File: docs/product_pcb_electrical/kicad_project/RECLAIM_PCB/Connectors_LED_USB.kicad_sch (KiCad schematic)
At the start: 15 parts, among them U11 PT4115

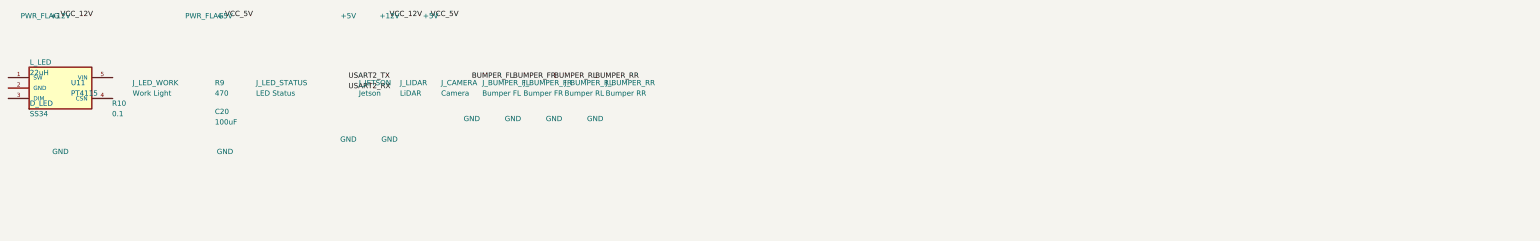
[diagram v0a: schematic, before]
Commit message: Add prototype schematic + tighten product layout to A3
Product: All 4 sub-sheets resized A2/A1→A3, components repositioned
into tight logical groups, duplicate K1/Q1 removed.

Prototype: New KiCad project with 3 hierarchical sheets
(Power, Teensy/Motor Control, Peripherals/Sensors), BOM, and
netlist reflecting as-built wiring: MD13C R3 + BTS7960 asymmetric
drivers, DC disconnect, 6-way fuse block, XINGYHENG servo buck.

Co-Authored-By: Claude Opus 4.6 <noreply@anthropic.com>
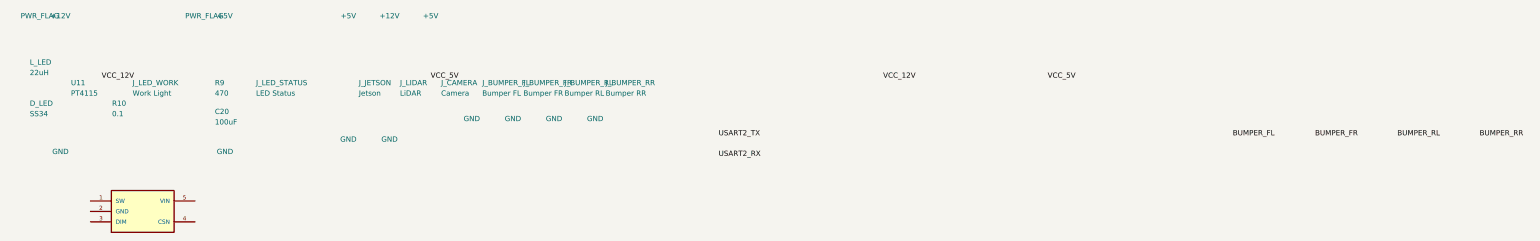
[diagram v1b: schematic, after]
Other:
- moved on the sheet: U11
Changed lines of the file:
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@@
 	(generator "eeschema")
 	(generator_version "10.0")
-	(paper "A2")
+	(paper "A3")
 	(title_block
 		(title "RECLAIM Product PCB - Connectors, LED, USB & Peripherals")
@@
 	(symbol
 		(lib_id "PT4115:PT4115")
-		(at 40 40 0)
+		(at 60 70 0)
 		(unit 1)
 		(body_style 1)
@@
 	(symbol
 		(lib_id "Device:L")
-		(at 30 35 0)
+		(at 45 52 0)
 		(unit 1)
 		(body_style 1)
@@
 	(symbol
 		(lib_id "Diode:SS34")
-		(at 30 45 0)
+		(at 45 95 0)
 		(unit 1)
 		(body_style 1)
@@
 	(symbol
 		(lib_id "Device:R")
-		(at 50 45 0)
+		(at 78 95 0)
 		(unit 1)
 		(body_style 1)
@@
 	(symbol
 		(lib_id "Connector_Generic:Conn_01x02")
-		(at 55 40 0)
+		(at 92 70 0)
 		(unit 1)
 		(body_style 1)
@@
 	(symbol
 		(lib_id "Device:R")
-		(at 75 40 0)
+		(at 130 55 0)
 		(unit 1)
 		(body_style 1)
@@
 	(symbol
 		(lib_id "Device:C")
-		(at 75 47 0)
+		(at 130 85 0)
 		(unit 1)
 		(body_style 1)
@@
 	(symbol
 		(lib_id "Connector_Generic:Conn_01x03")
-		(at 85 40 0)
+		(at 150 65 0)
 		(unit 1)
 		(body_style 1)
@@
 	(symbol
 		(lib_id "Connector_Generic:Conn_01x04")
-		(at 110 40 0)
+		(at 200 60 0)
 		(unit 1)
 		(body_style 1)
@@
 	(symbol
 		(lib_id "Connector_Generic:Conn_01x04")
-		(at 120 40 0)
+		(at 245 60 0)
 		(unit 1)
 		(body_style 1)
@@
 	(symbol
 		(lib_id "Connector_Generic:Conn_01x02")
-		(at 130 40 0)
+		(at 285 60 0)
 		(unit 1)
 		(body_style 1)
@@
 	(symbol
 		(lib_id "Connector_Generic:Conn_01x02")
-		(at 140 40 0)
+		(at 325 60 0)
 		(unit 1)
 		(body_style 1)
@@
 	(symbol
 		(lib_id "Connector_Generic:Conn_01x02")
-		(at 150 40 0)
+		(at 345 60 0)
 		(unit 1)
 		(body_style 1)
@@
 	(symbol
 		(lib_id "Connector_Generic:Conn_01x02")
-		(at 160 40 0)
+		(at 365 60 0)
 		(unit 1)
 		(body_style 1)
@@
 	(symbol
 		(lib_id "Connector_Generic:Conn_01x02")
-		(at 170 40 0)
+		(at 385 60 0)
 		(unit 1)
 		(body_style 1)
@@
 	(symbol
 		(lib_id "power:+12V")
-		(at 40 25 0)
+		(at 50 30 0)
 		(unit 1)
 		(body_style 1)
@@
 	(symbol
 		(lib_id "power:+5V")
-		(at 80 25 0)
+		(at 130 30 0)
 		(unit 1)
 		(body_style 1)
@@
 	(symbol
 		(lib_id "power:+5V")
-		(at 110 25 0)
+		(at 195 30 0)
 		(unit 1)
 		(body_style 1)
@@
 	(symbol
 		(lib_id "power:+12V")
-		(at 120 25 0)
+		(at 240 30 0)
 		(unit 1)
 		(body_style 1)
@@
 	(symbol
 		(lib_id "power:+5V")
-		(at 130 25 0)
+		(at 280 30 0)
 		(unit 1)
 		(body_style 1)
@@
 	(symbol
 		(lib_id "power:GND")
-		(at 40 58 0)
+		(at 50 130 0)
 		(unit 1)
 		(body_style 1)
@@
 	(symbol
 		(lib_id "power:GND")
-		(at 80 58 0)
+		(at 130 115 0)
 		(unit 1)
 		(body_style 1)
@@
 	(symbol
 		(lib_id "power:GND")
-		(at 110 55 0)
+		(at 195 100 0)
 		(unit 1)
 		(body_style 1)
@@
 	(symbol
 		(lib_id "power:GND")
-		(at 120 55 0)
+		(at 240 100 0)
 		(unit 1)
 		(body_style 1)
@@
 	(symbol
 		(lib_id "power:GND")
-		(at 140 50 0)
+		(at 325 95 0)
 		(unit 1)
 		(body_style 1)
@@
 	(symbol
 		(lib_id "power:GND")
-		(at 150 50 0)
+		(at 345 95 0)
 		(unit 1)
 		(body_style 1)
@@
 	(symbol
 		(lib_id "power:GND")
-		(at 160 50 0)
+		(at 365 95 0)
 		(unit 1)
 		(body_style 1)
@@
 	(symbol
 		(lib_id "power:GND")
-		(at 170 50 0)
+		(at 385 95 0)
 		(unit 1)
 		(body_style 1)
@@
 	(symbol
 		(lib_id "power:PWR_FLAG")
-		(at 35 25 0)
+		(at 58 30 0)
 		(unit 1)
 		(body_style 1)
@@
 	(symbol
 		(lib_id "power:PWR_FLAG")
-		(at 75 25 0)
+		(at 138 30 0)
 		(unit 1)
 		(body_style 1)
@@
 	)
 	(label "VCC_12V"
-		(at 40 23 0)
+		(at 50 38 0)
 		(fields_autoplaced yes)
 		(effects
@@
 	)
 	(label "VCC_5V"
-		(at 80 23 0)
+		(at 130 38 0)
 		(fields_autoplaced yes)
 		(effects
@@
 	)
 	(label "USART2_TX"
-		(at 110 38 0)
+		(at 200 52 0)
 		(fields_autoplaced yes)
 		(effects
@@
 	)
 	(label "USART2_RX"
-		(at 110 40.54 0)
+		(at 200 57 0)
 		(fields_autoplaced yes)
 		(effects
@@
 	)
 	(label "VCC_12V"
-		(at 120 23 0)
+		(at 240 38 0)
 		(fields_autoplaced yes)
 		(effects
@@
 	)
 	(label "VCC_5V"
-		(at 130 23 0)
+		(at 280 38 0)
 		(fields_autoplaced yes)
 		(effects
@@
 	)
 	(label "BUMPER_FL"
-		(at 140 38 0)
+		(at 325 52 0)
 		(fields_autoplaced yes)
 		(effects
@@
 	)
 	(label "BUMPER_FR"
-		(at 150 38 0)
+		(at 345 52 0)
 		(fields_autoplaced yes)
 		(effects
@@
 	)
 	(label "BUMPER_RL"
-		(at 160 38 0)
+		(at 365 52 0)
 		(fields_autoplaced yes)
 		(effects
@@
 	)
 	(label "BUMPER_RR"
-		(at 170 38 0)
+		(at 385 52 0)
 		(fields_autoplaced yes)
 		(effects
